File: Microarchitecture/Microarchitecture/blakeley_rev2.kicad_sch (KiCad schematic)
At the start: 15 parts

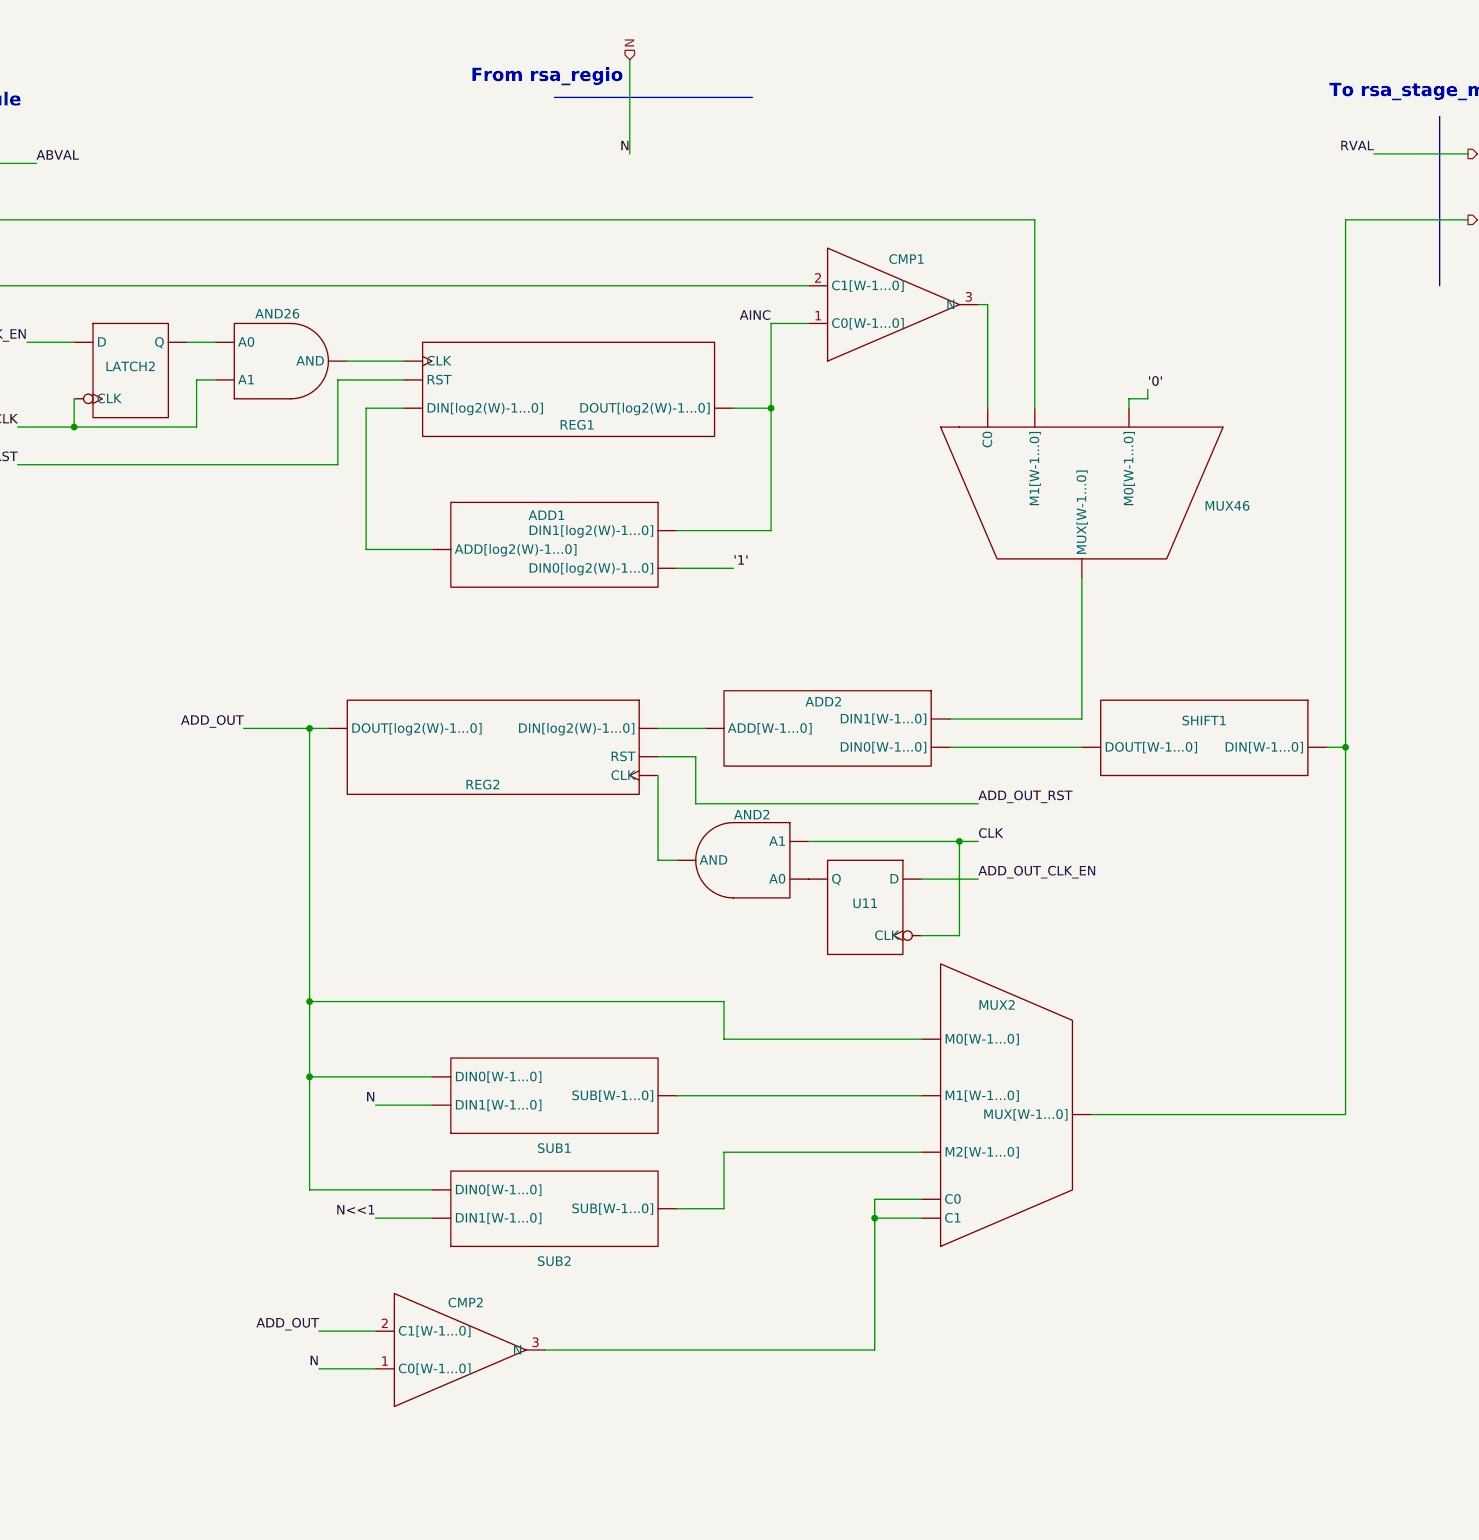
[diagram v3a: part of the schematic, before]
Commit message: Added suport for num_pipeline_stages neq 2**x
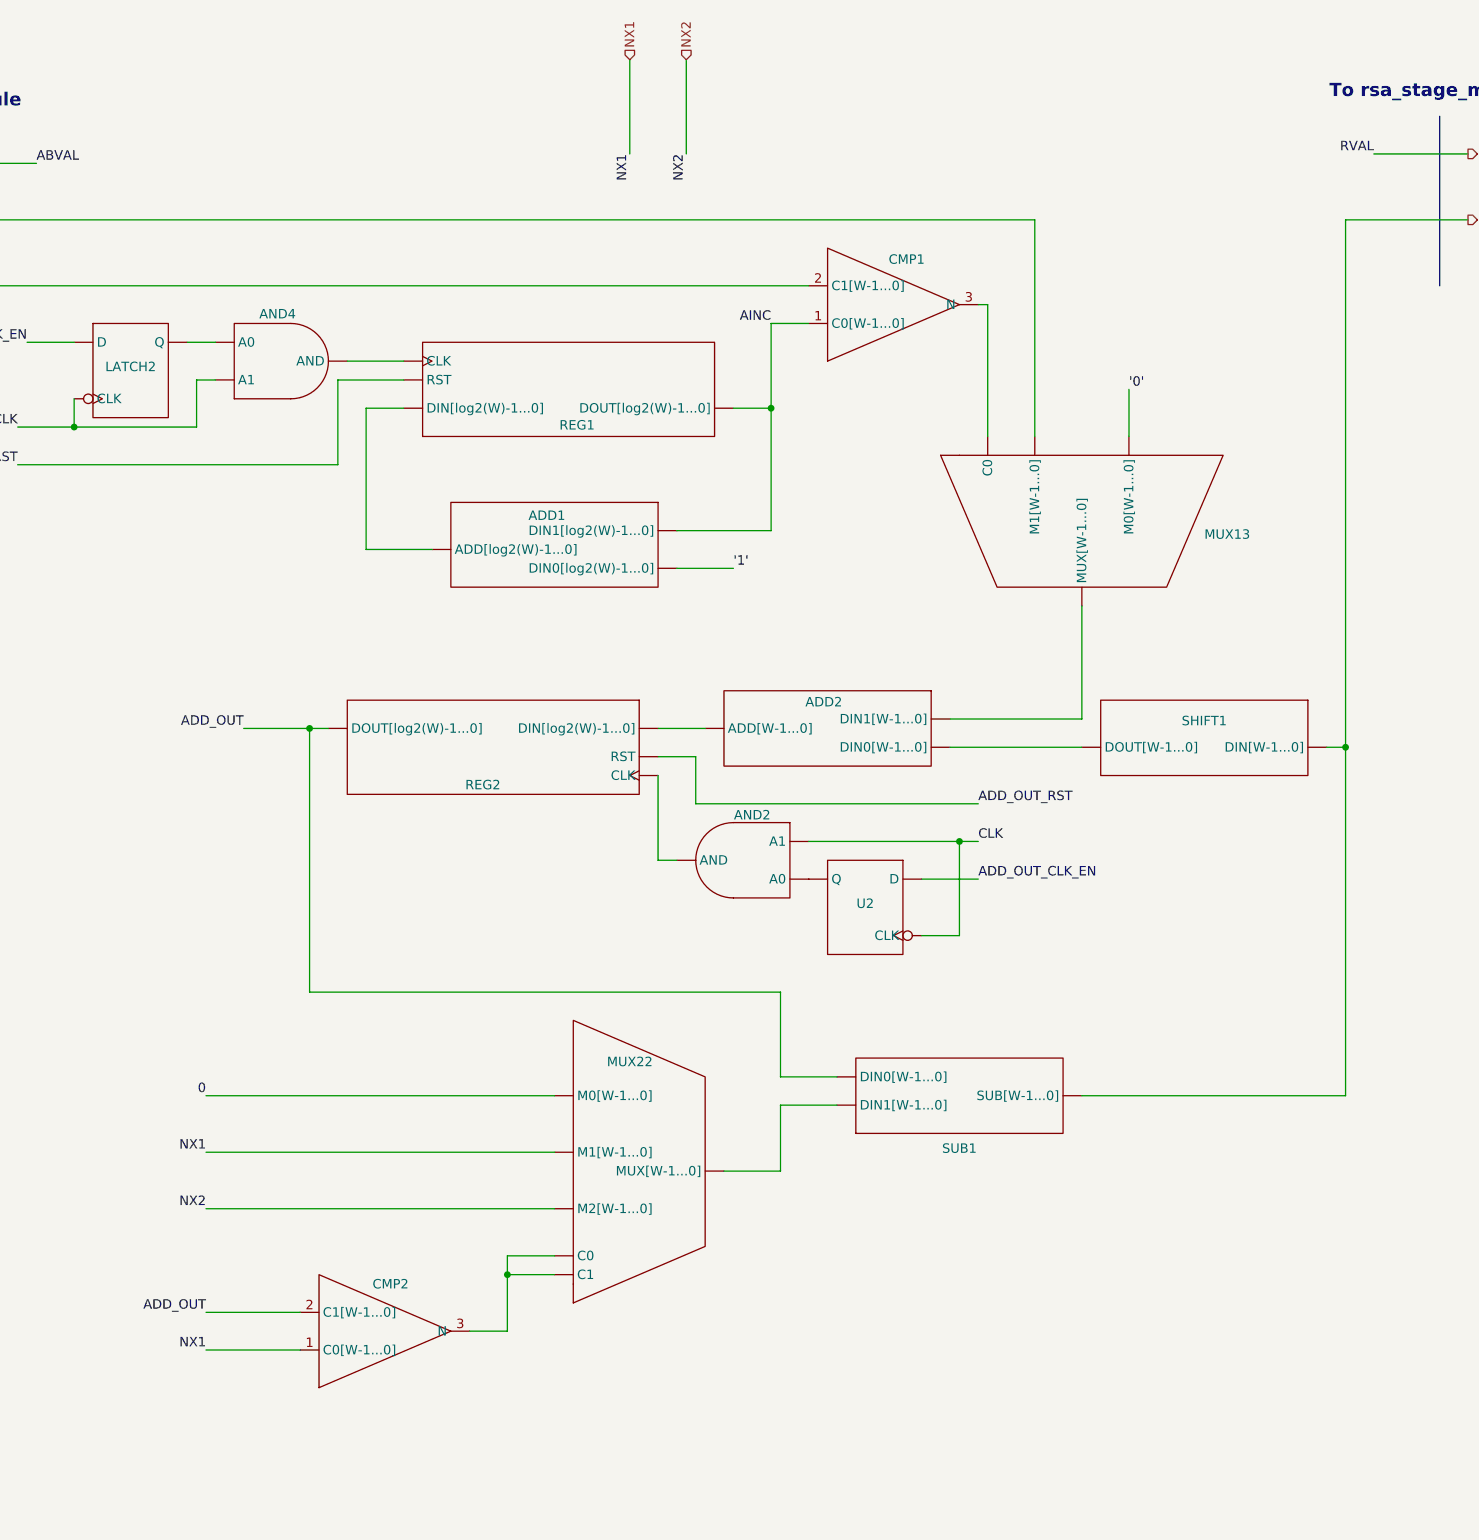
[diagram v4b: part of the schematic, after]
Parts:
- removed MUX2: ~, symbol Symbols:MUX_BUS
- removed SUB2: ~, symbol Symbols:ADD
- added MUX22: ~, symbol Symbols:MUX_BUS
- renumbered AND26 to AND4, MUX46 to MUX13, U11 to U2
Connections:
- net R: now also SUB1. (SUB[W-1...0])
- net at ADD2. (DIN1[W-1...0]): now also SHIFT1. (DOUT[W-1...0]); no longer MUX13. (MUX[W-1...0])
- net at CMP2.3 (N): now also MUX22. (MUX[W-1...0])
- net N renamed NX1
- net NX1: now also MUX22. (MUX[W-1...0]); no longer SUB1. (SUB[W-1...0])
- new net: AND2. (AND), REG2. (RST)
- new net: AND2. (AND), U2. (Q)
- new net: AND4. (AND), LATCH2. (Q)
- new net: MUX22. (MUX[W-1...0]), SUB1. (SUB[W-1...0])
- new net: AND4. (AND), REG1. (RST)
- new net: ADD2. (DIN1[W-1...0]), MUX13. (MUX[W-1...0])
- new net: ADD2. (DIN1[W-1...0]), REG2. (RST)
- new net: ADD1. (DIN1[log2(W)-1...0]), REG1. (RST)
- new net 0: MUX22. (MUX[W-1...0])
- new net NX2: MUX22. (MUX[W-1...0])
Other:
- note removed: "From rsa_regio"
- moved on the sheet: CMP2, MUX13, SUB1

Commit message: Tried to update tb
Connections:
- net at ADD2. (DIN1[W-1...0]): now also SHIFT1. (DOUT[W-1...0]); no longer MUX13. (MUX[W-1...0])
- new net: AND2. (AND), REG2. (RST)
- new net: AND2. (AND), U2. (Q)
- new net: AND4. (AND), LATCH2. (Q)
- new net: MUX22. (MUX[W-1...0]), SUB1. (SUB[W-1...0])
- new net: AND4. (AND), REG1. (RST)
- new net: ADD2. (DIN1[W-1...0]), MUX13. (MUX[W-1...0])
- new net: ADD2. (DIN1[W-1...0]), REG2. (RST)
- new net: ADD1. (DIN1[log2(W)-1...0]), REG1. (RST)
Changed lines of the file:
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@@
+		)
+	)
+	(polyline
+		(pts
+			(xy 256.54 36.83) (xy 278.13 36.83)
+		)
+		(stroke
+			(width 0)
+			(type default)
 		)
 	)
@@
 		)
 	)
+	(text "From rsa_stage_module"
+		(exclude_from_sim no)
+		(at 243.078 33.782 0)
+		(effects
+			(font
+				(size 1.778 1.778)
+				(thickness 0.3556)
+				(bold yes)
+			)
+		)
+	)
